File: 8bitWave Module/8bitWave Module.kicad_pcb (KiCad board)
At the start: 2 copper layers, 99.7 x 64.1 mm, 54 parts, among them IC1 0.96_I2C_OLED, J1 REM, J2 EAR, J3 EXTENSION, J4 DC IN, J5 LP_FILTER, J6 SPI, J7 EAR_SEL, M1 Mounting, M2 Mounting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

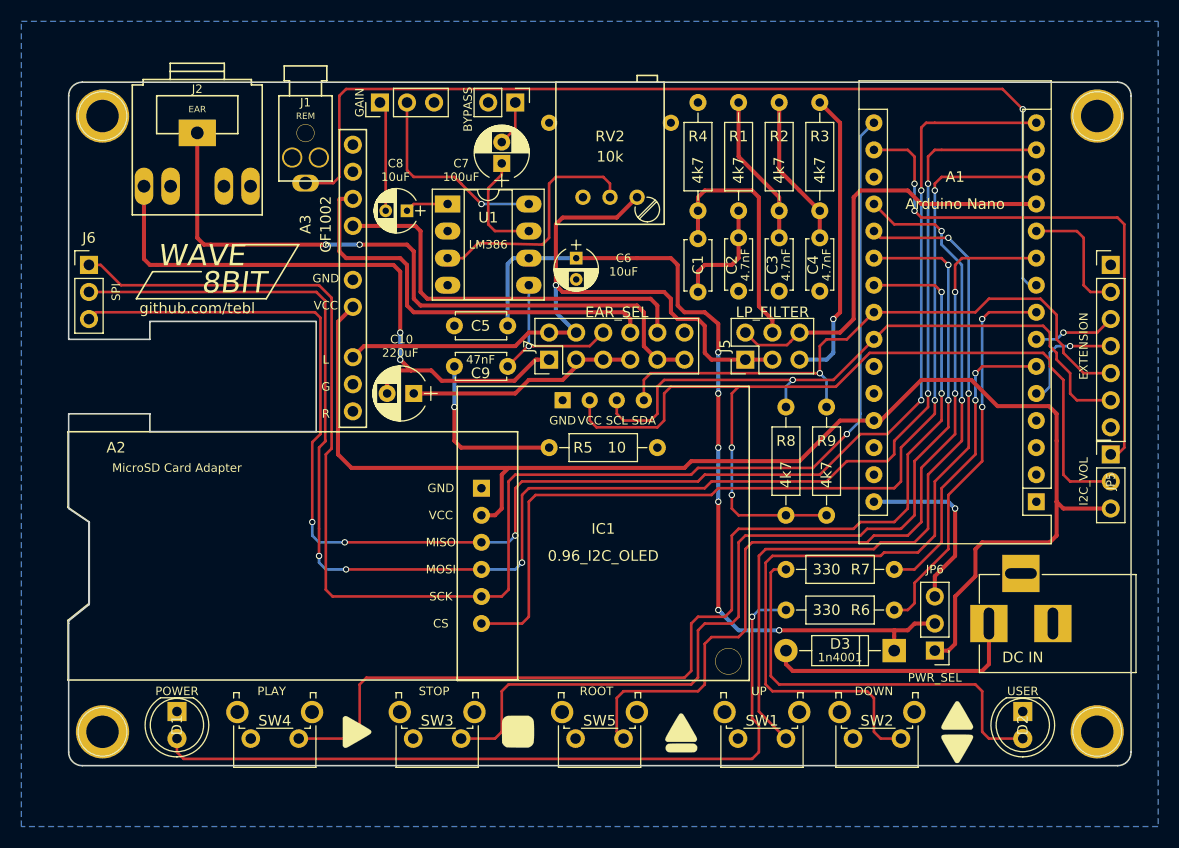
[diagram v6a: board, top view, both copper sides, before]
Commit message: Added bypass cap
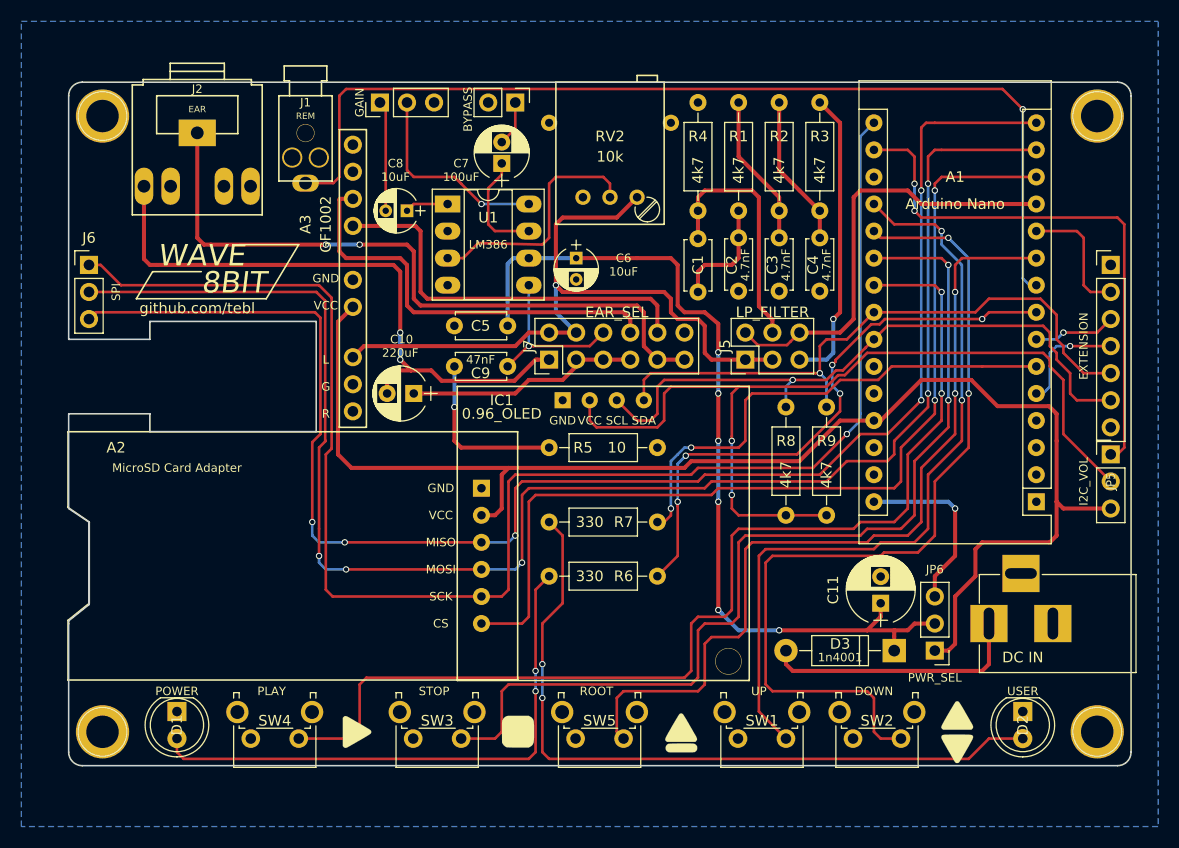
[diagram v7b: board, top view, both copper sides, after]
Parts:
- added C11: 220uF, Capacitors_THT:CP_Radial_D6.3mm_P2.50mm, F.Cu at (146.7, 127.0)
- IC1: value 0.96_I2C_OLED -> 0.96_OLED
- moved R7 22.7 mm to (115.6, 119.4)
- moved R6 22.5 mm to (115.6, 124.5)
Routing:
- net Net-(D2-Pad2): track 39.6 -> 69.0 mm, vias 0 -> 2
- net Net-(D1-Pad2): track 72.8 -> 52.5 mm, vias 1 -> 2
- net /USER: track 28.7 -> 46.8 mm
- net /POWER: track 36.8 -> 54.6 mm, vias 2 -> 5
- net VEXT: track 80.7 -> 83.7 mm
- net Net-(IC1-Pad2): track 86.9 -> 84.6 mm
- net /SCL: track 61.0 -> 60.2 mm

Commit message: Updated module (KiCad 5)
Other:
- rule pad_to_mask_clearance: 0.2 -> 0
